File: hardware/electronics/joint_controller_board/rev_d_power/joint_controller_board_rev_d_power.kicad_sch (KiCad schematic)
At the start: 34 parts, among them J1 J_IFACE, J2 J_PWR_IN_RAW, J3 J_PWR_CHAIN_RAW, J4 J_PWR_OUT_SW, Q1 BSC016N06NS, Q2 BSC016N06NS, U1 TPS2492PW, U2 LMR36520DDA, U3 TLV75533PDBV

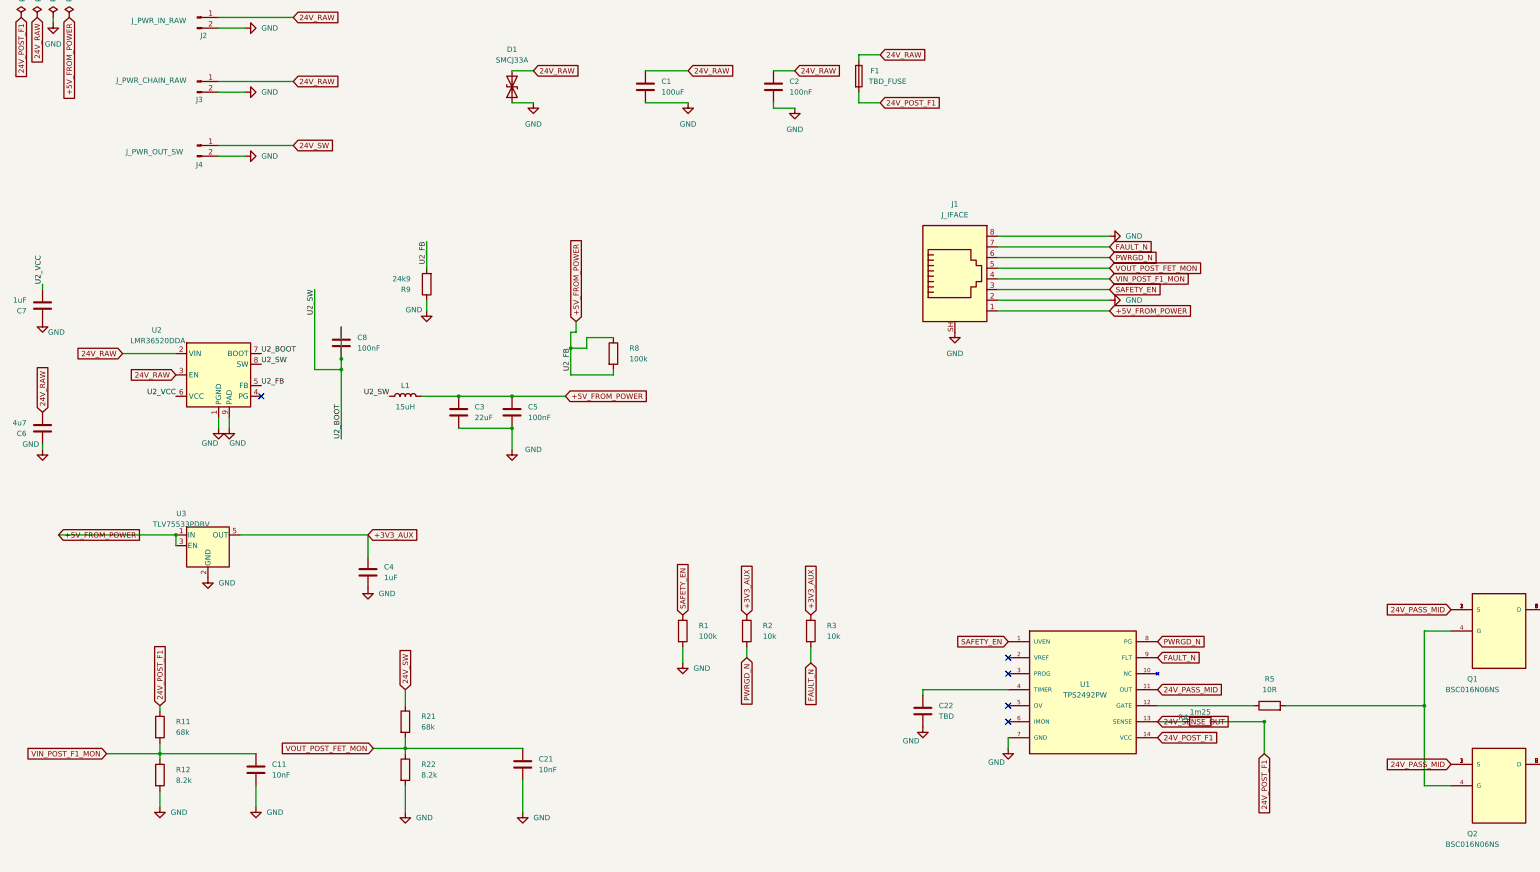
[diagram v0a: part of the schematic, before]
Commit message: feat: refine rev d power protection and buck
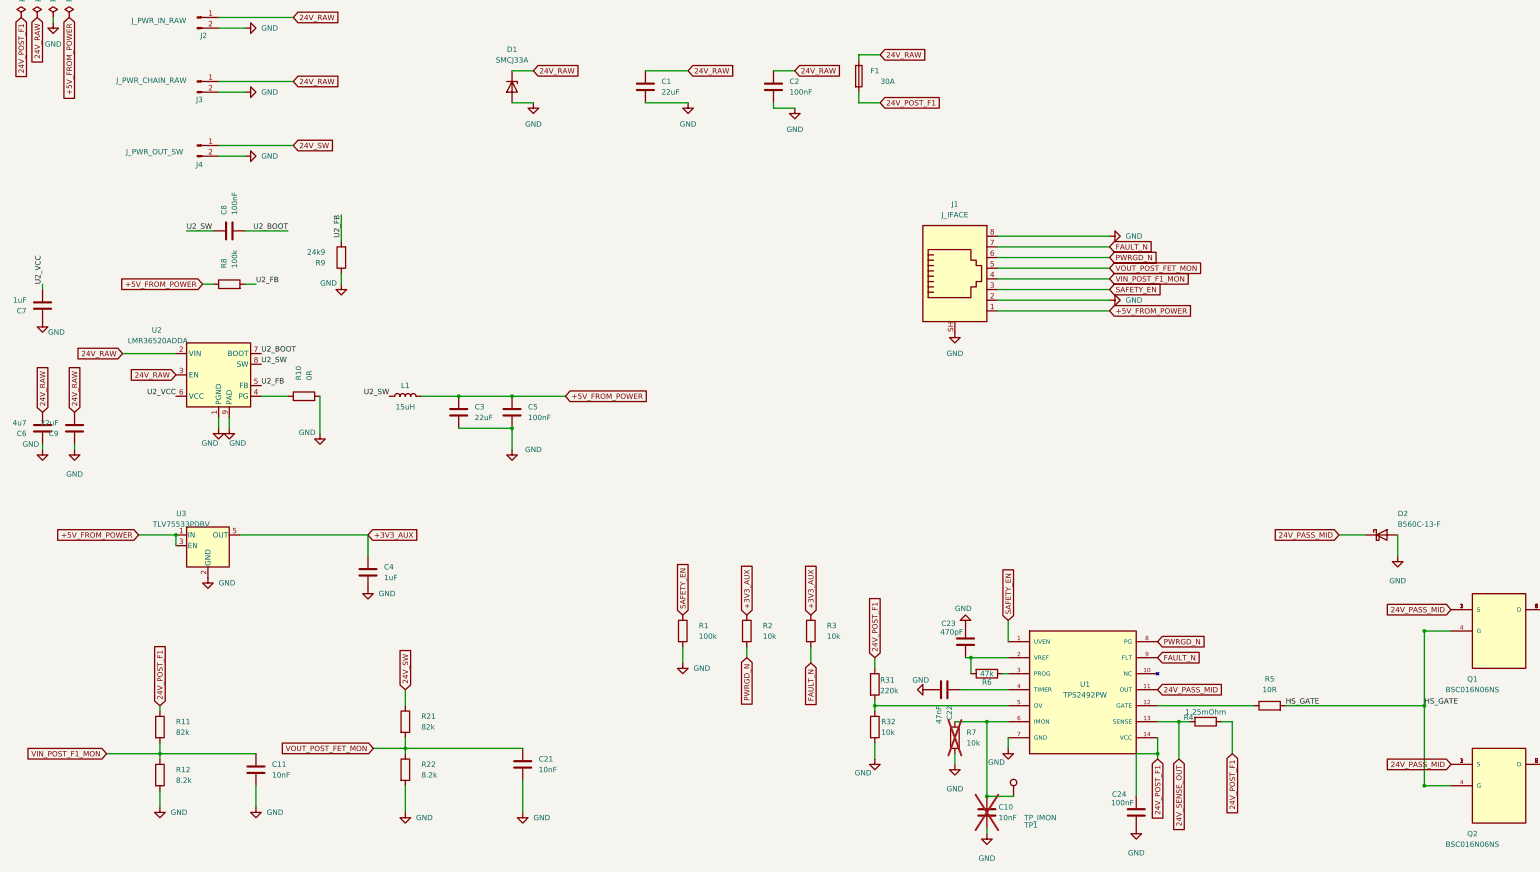
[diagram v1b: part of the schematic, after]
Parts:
- added C10: 10nF, Capacitor_SMD:C_0805_2012Metric, symbol Device:C
- added C23: 470pF, Capacitor_SMD:C_0805_2012Metric, symbol Device:C
- added C24: 100nF, Capacitor_SMD:C_0805_2012Metric, symbol Device:C
- added C9: 22uF, Capacitor_SMD:C_1210_3225Metric, symbol Device:C
- added D2: B560C-13-F, Diode_SMD:D_SMB, symbol Device:D_Schottky
- added R10: 0R, Resistor_SMD:R_0805_2012Metric, symbol Device:R
- added R31: 220k, Resistor_SMD:R_0805_2012Metric, symbol Device:R
- added R32, R7: 10k, Resistor_SMD:R_0805_2012Metric, symbol Device:R
- added R6: 47k, Resistor_SMD:R_0805_2012Metric, symbol Device:R
- added TP1: TP_IMON, TestPoint:TestPoint_Pad_D1.5mm, symbol Connector:TestPoint
- C1: value 100uF -> 22uF
- C22: value TBD -> 47nF
- D1: symbol Device:D_TVS -> Device:D_Zener; MPN (none) -> SMCJ33A; Manufacturer (none) -> Littelfuse
- F1: value TBD_FUSE -> 30A; footprint (none) -> Fuse:Fuseholder_Blade_ATO_Littelfuse_FLR_178.6165; MPN (none) -> FLR178.6165; Manufacturer (none) -> Littelfuse
- J1: MPN (none) -> RJHSE-5380; Manufacturer (none) -> Amphenol Commercial Products
- J2: MPN (none) -> XT60PW-M; Manufacturer (none) -> AMASS
- J3, J4: MPN (none) -> XT60PW-F; Manufacturer (none) -> AMASS
- L1: footprint (none) -> Inductor_SMD:L_Bourns_SRP5030T; MPN (none) -> SRP5030T-150M; Manufacturer (none) -> Bourns
- Q1, Q2: MPN (none) -> BSC016N06NSATMA1; Manufacturer (none) -> Infineon
- R11, R21: value 68k -> 82k
- R4: value 1m25 -> 1.25mOhm; MPN (none) -> WSR21L250FEA; Manufacturer (none) -> Vishay Dale
- U1: MPN (none) -> TPS2492PW; Manufacturer (none) -> Texas Instruments
- U2: value LMR36520DDA -> LMR36520ADDA; symbol Regulator_Switching:LMR36510ADDA -> rev_d_power_parts:LMR36520ADDA; MPN (none) -> LMR36520ADDAR; Manufacturer (none) -> Texas Instruments
- U3: symbol Regulator_Linear:TLV70012_SOT23-5 -> Regulator_Linear:TLV75533PDBV; MPN (none) -> TLV75533PDBVR; Manufacturer (none) -> Texas Instruments
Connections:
- net +5V_FROM_POWER: no longer R8.2, R9.2, U2.5 (FB)
- net 24V_PASS_MID: now also D2.1 (K)
- net 24V_POST_F1: now also C24.2, R31.1
- net 24V_RAW: now also D1.1 (K), C9.2; no longer D1.2 (A2)
- net GND: now also D1.2 (A), C10.2, C23.2, C24.1, C9.1, D2.2 (A), R10.2, R32.2, R7.2; no longer D1.1 (A1)
- net U2_BOOT: no longer C8.1, L1.1, U2.8 (SW)
- net at U2.4 (PG): now also R10.1
- net at U1.2 (VREF): now also C23.1, R6.2
- net at U1.3 (PROG): now also R6.1
- net at U1.5 (OV): now also R31.2, R32.1
- net at U1.6 (IMON): now also C10.1, R7.1, TP1.1
- net HS_GATE: now reaches Q1.4 (G), Q2.4 (G), R5.2
- new net U2_FB: R8.2, R9.2, U2.5 (FB)
- new net U2_SW: C8.1, L1.1, U2.8 (SW)
- no-connect marks 5 -> 0
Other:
- moved on the sheet: C22, C8, D1, R4, R8, R9

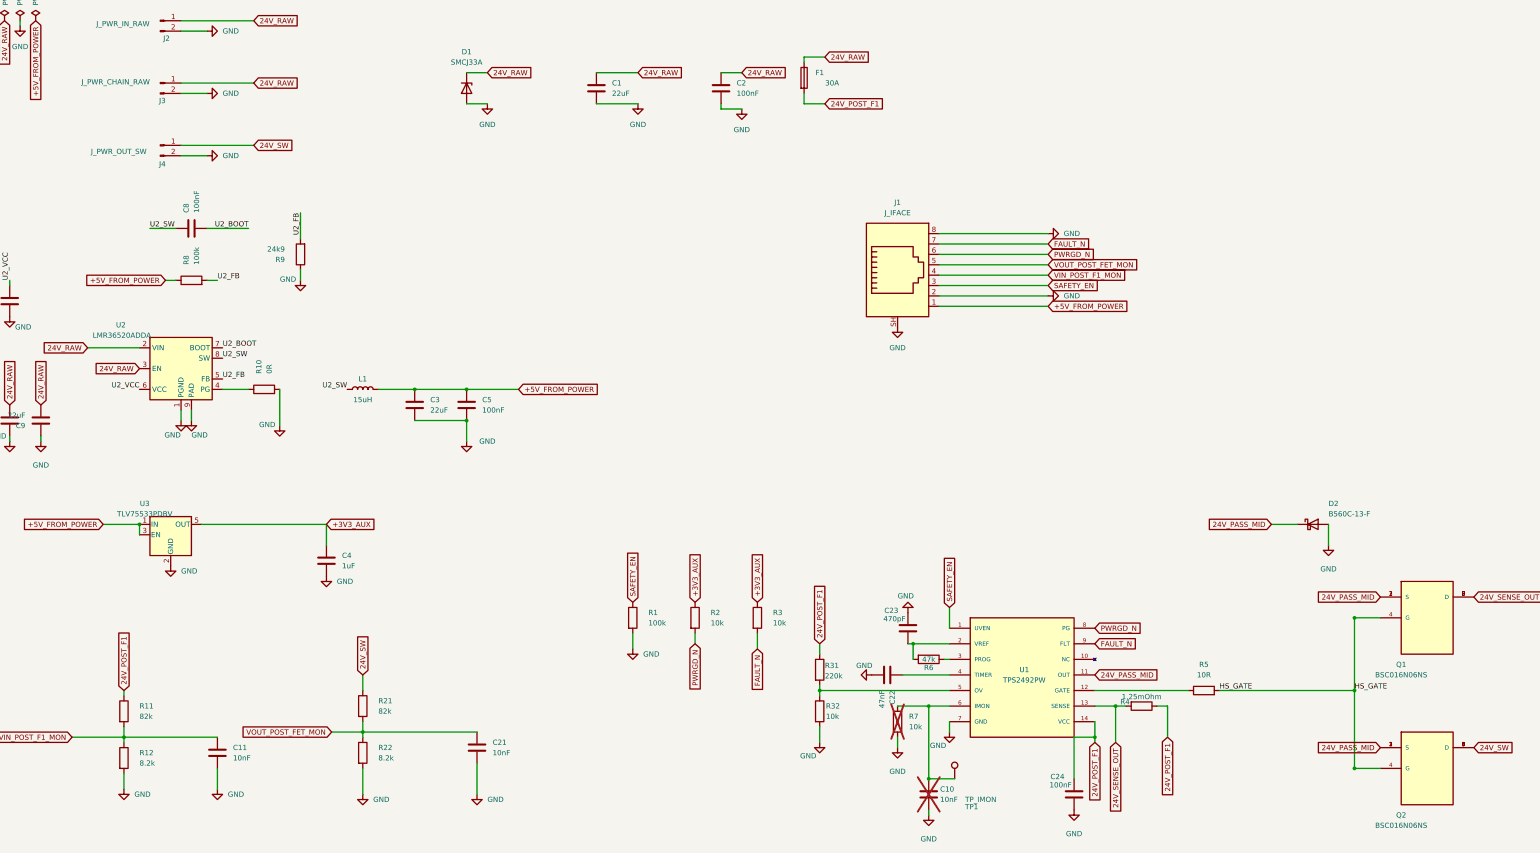
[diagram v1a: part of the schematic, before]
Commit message: feat(rev_d_power): multi-layer power zones + TPS2492 control hardening
Replace discrete power traces with multi-layer zones on 24V_RAW,
24V_POST_F1, 24V_SENSE_OUT, 24V_PASS_MID, 24V_SW: lower impedance
and better heat spreading on the 22A continuous path.

Schematic/control:
- C22 TIMER 47nF -> 10nF (~1.5ms) to keep Q1/Q2 inside SOA on hard short
- R6 47k VREF-PROG disables constant-power engine per TPS2492 DS p.8
- Remove TP1/R7/C10 IMON debug set; add no_connect on U1 pin 6
- BSC016N06NS symbol: drop duplicate drain pins (fix duplicate_pins ERC)

Layout/verification:
- GND zone continuity kept on both layers plus stitching vias
- 4 thermal vias on 24V_PASS_MID with F.Cu heat-spreader island
- 16-via array on Q2 -> J4 for 24V_SW cross-layer transition
- DRU exception for U2 HTSOP exposed pad mask bridges (standard TI layout)
- Reference text moved to Fab layer to clean silk overlap warnings

Result: ERC 0, DRC 0, 0 unconnected items. Ready for gerber export.
Signed-off-by: graceful-kinematics <info@aliahumanoid.com>
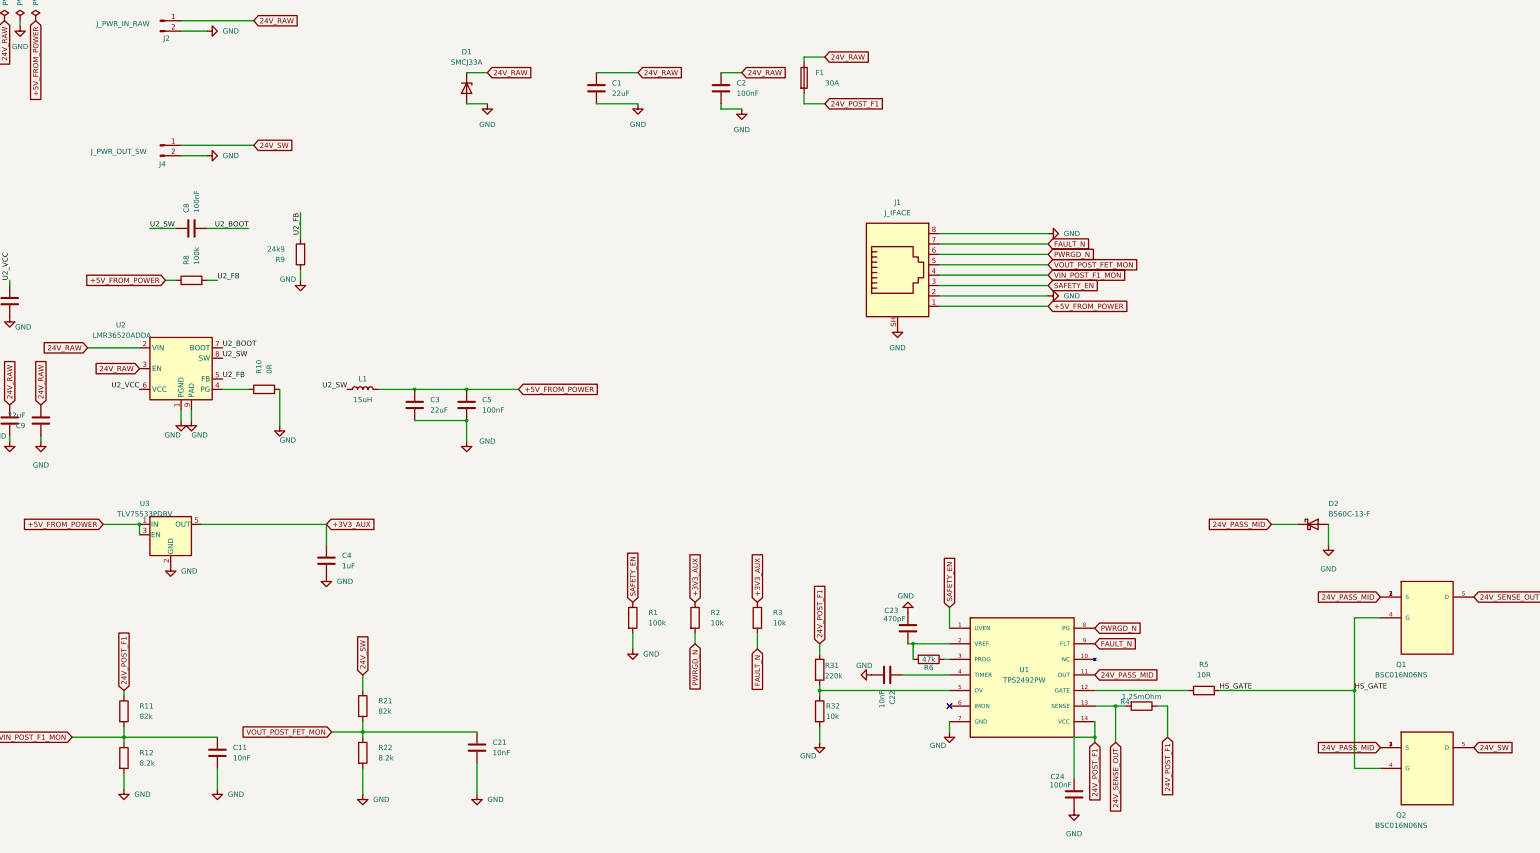
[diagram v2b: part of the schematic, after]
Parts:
- removed C10: 10nF, Capacitor_SMD:C_0805_2012Metric, symbol Device:C
- removed J3: J_PWR_CHAIN_RAW, Connector_AMASS:AMASS_XT60PW-F_1x02_P7.20mm_Horizontal, symbol Connector:Conn_01x02_Pin
- removed R7: 10k, Resistor_SMD:R_0805_2012Metric, symbol Device:R
- removed TP1: TP_IMON, TestPoint:TestPoint_Pad_D1.5mm, symbol Connector:TestPoint
- C22: value 47nF -> 10nF
- F1: footprint Fuse:Fuseholder_Blade_ATO_Littelfuse_FLR_178.6165 -> rev_d_power_footprints:FuseHolder_Blade_ATO_Littelfuse_FLR_178.6165
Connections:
- net 24V_SENSE_OUT: no longer Q1.6 (D), Q1.7 (D), Q1.8 (D)
- net 24V_SW: no longer Q2.6 (D), Q2.7 (D), Q2.8 (D)
- no-connect marks 0 -> 1

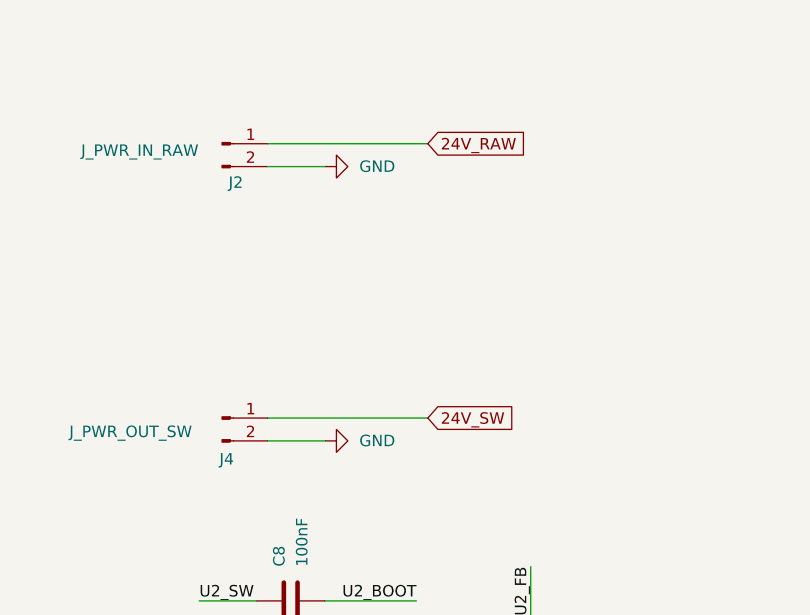
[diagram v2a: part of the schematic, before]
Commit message: fix(rev_d_power): correct XT60 polarity pin assignment on J2/J4
Critical electrical fix: the AMASS XT60PW KiCad footprint convention
is pad 1 = negative (angled side), pad 2 = positive (flat side). The
schematic had the reversed assignment (pin 1 = 24V, pin 2 = GND) which
would have short-circuited the battery through the board on first power-up
since the XT60 housing is mechanically polarized and forces contact mating
to the physically marked + side.

Changes:
- J2 (XT60PW-M, 24V input): pin 1 -> GND, pin 2 -> 24V_RAW
- J4 (XT60PW-F, 24V switched output): pin 1 -> GND, pin 2 -> 24V_SW
- Re-loaded both footprints from stock KiCad library to restore correct
  pad local positions after polarity fix (pad 2 local X sign matches
  housing geometry: +7.2mm for M, -7.2mm for F)
- Moved refreshed silk elements to F.Fab layer on J2/J4 (matches the
  board-wide silk cleanup pattern used elsewhere)

Verification: rev_c (successfully fabricated) uses the same pin 1 = GND,
pin 2 = 24V assignment on XT60PW connectors, confirming the convention.

Result: ERC 0, DRC 0 violations, 0 unconnected items.
Signed-off-by: graceful-kinematics <info@aliahumanoid.com>
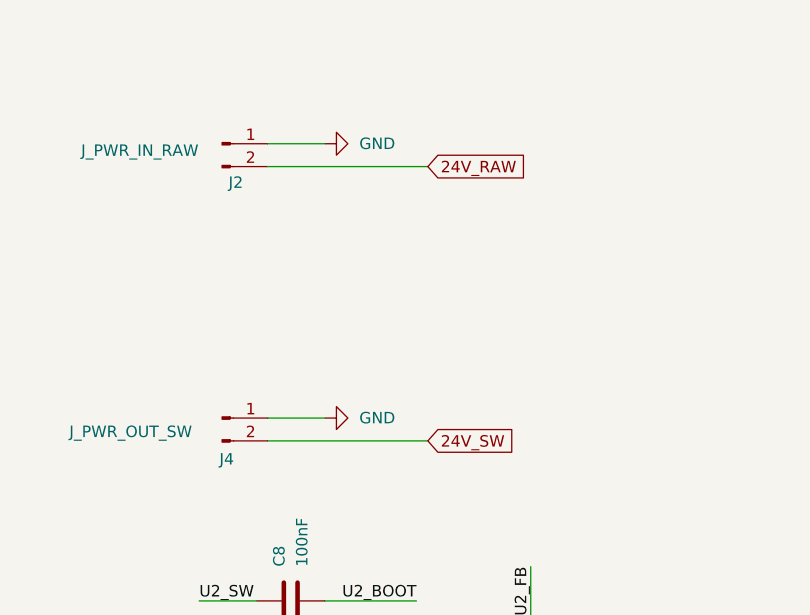
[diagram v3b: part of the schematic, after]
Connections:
- net 24V_RAW: now also J2.2 (Pin_2); no longer J2.1 (Pin_1)
- net 24V_SW: now also J4.2 (Pin_2); no longer J4.1 (Pin_1)
- net GND: now also J2.1 (Pin_1), J4.1 (Pin_1); no longer J2.2 (Pin_2), J4.2 (Pin_2)
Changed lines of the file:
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@@
 	(wire
 		(pts
-			(xy 67.31 29.21) (xy 85.09 29.21)
+			(xy 67.31 31.75) (xy 85.09 31.75)
 		)
 		(stroke
@@
 	(wire
 		(pts
-			(xy 67.31 62.23) (xy 73.66 62.23)
+			(xy 67.31 59.69) (xy 73.66 59.69)
 		)
 		(stroke
@@
 	(wire
 		(pts
-			(xy 67.31 59.69) (xy 85.09 59.69)
+			(xy 67.31 62.23) (xy 85.09 62.23)
 		)
 		(stroke
@@
 	(wire
 		(pts
-			(xy 67.31 31.75) (xy 73.66 31.75)
+			(xy 67.31 29.21) (xy 73.66 29.21)
 		)
 		(stroke
@@
 	(global_label "24V_RAW"
 		(shape input)
-		(at 85.09 29.21 0)
-		(fields_autoplaced yes)
-		(effects
-			(font
-				(size 1.27 1.27)
-			)
-			(justify left)
-		)
-		(property "Intersheetrefs" "${INTERSHEET_REFS}"
-			(at 85.09 29.21 0)
+		(at 85.09 31.75 0)
+		(fields_autoplaced yes)
+		(effects
+			(font
+				(size 1.27 1.27)
+			)
+			(justify left)
+		)
+		(property "Intersheetrefs" "${INTERSHEET_REFS}"
+			(at 85.09 31.75 0)
 			(effects
 				(font
@@
 	(global_label "24V_SW"
 		(shape input)
-		(at 85.09 59.69 0)
-		(fields_autoplaced yes)
-		(effects
-			(font
-				(size 1.27 1.27)
-			)
-			(justify left)
-		)
-		(property "Intersheetrefs" "${INTERSHEET_REFS}"
-			(at 85.09 59.69 0)
+		(at 85.09 62.23 0)
+		(fields_autoplaced yes)
+		(effects
+			(font
+				(size 1.27 1.27)
+			)
+			(justify left)
+		)
+		(property "Intersheetrefs" "${INTERSHEET_REFS}"
+			(at 85.09 62.23 0)
 			(effects
 				(font
@@
 	(symbol
 		(lib_id "power:GND")
-		(at 73.66 31.75 90)
+		(at 73.66 29.21 90)
 		(unit 1)
 		(exclude_from_sim no)
@@
 		(fields_autoplaced yes)
 		(property "Reference" "#PWR001"
-			(at 80.01 31.75 0)
+			(at 80.01 29.21 0)
 			(effects
 				(font
@@
 		)
 		(property "Value" "GND"
-			(at 77.47 31.7499 90)
+			(at 77.47 29.2099 90)
 			(effects
 				(font
@@
 		)
 		(property "Footprint" ""
-			(at 73.66 31.75 0)
+			(at 73.66 29.21 0)
 			(effects
 				(font
@@
 		)
 		(property "Datasheet" ""
-			(at 73.66 31.75 0)
+			(at 73.66 29.21 0)
 			(effects
 				(font
@@
 		)
 		(property "Description" "Power symbol creates a global label with name \"GND\" , ground"
-			(at 73.66 31.75 0)
+			(at 73.66 29.21 0)
 			(effects
 				(font
@@
 	(symbol
 		(lib_id "power:GND")
-		(at 73.66 62.23 90)
+		(at 73.66 59.69 90)
 		(unit 1)
 		(exclude_from_sim no)
@@
 		(fields_autoplaced yes)
 		(property "Reference" "#PWR003"
-			(at 80.01 62.23 0)
+			(at 80.01 59.69 0)
 			(effects
 				(font
@@
 		)
 		(property "Value" "GND"
-			(at 77.47 62.2299 90)
+			(at 77.47 59.6899 90)
 			(effects
 				(font
@@
 		)
 		(property "Footprint" ""
-			(at 73.66 62.23 0)
+			(at 73.66 59.69 0)
 			(effects
 				(font
@@
 		)
 		(property "Datasheet" ""
-			(at 73.66 62.23 0)
+			(at 73.66 59.69 0)
 			(effects
 				(font
@@
 		)
 		(property "Description" "Power symbol creates a global label with name \"GND\" , ground"
-			(at 73.66 62.23 0)
-			(effects
-				(font
+			(at 73.66 59.69 0)
+			(effects
+				(font
